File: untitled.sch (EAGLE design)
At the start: 22 parts, among them J3 CORTEX_DEBUG_PTH, J6 USB-MICROB, U1 ATSAMD21G-M, U2 MIC5501-3.0YM5-TR, U3 TPD2S017

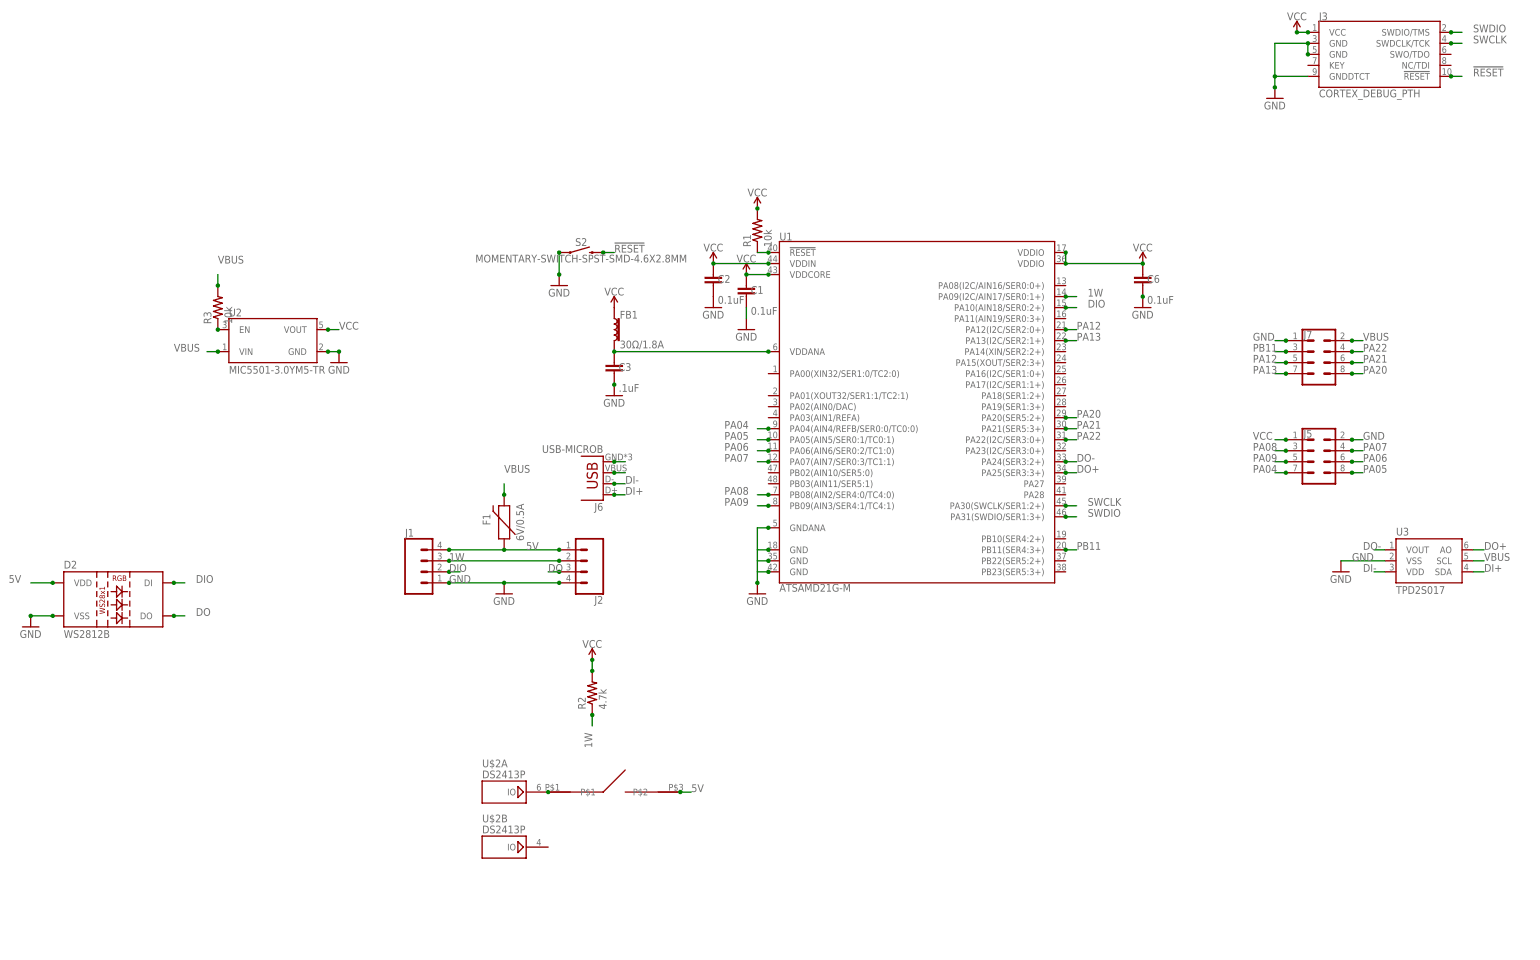
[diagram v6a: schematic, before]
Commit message: Updated Routing
Updated routing to remove vias. Changed switch wiring to reflect ds2413 example circuit.
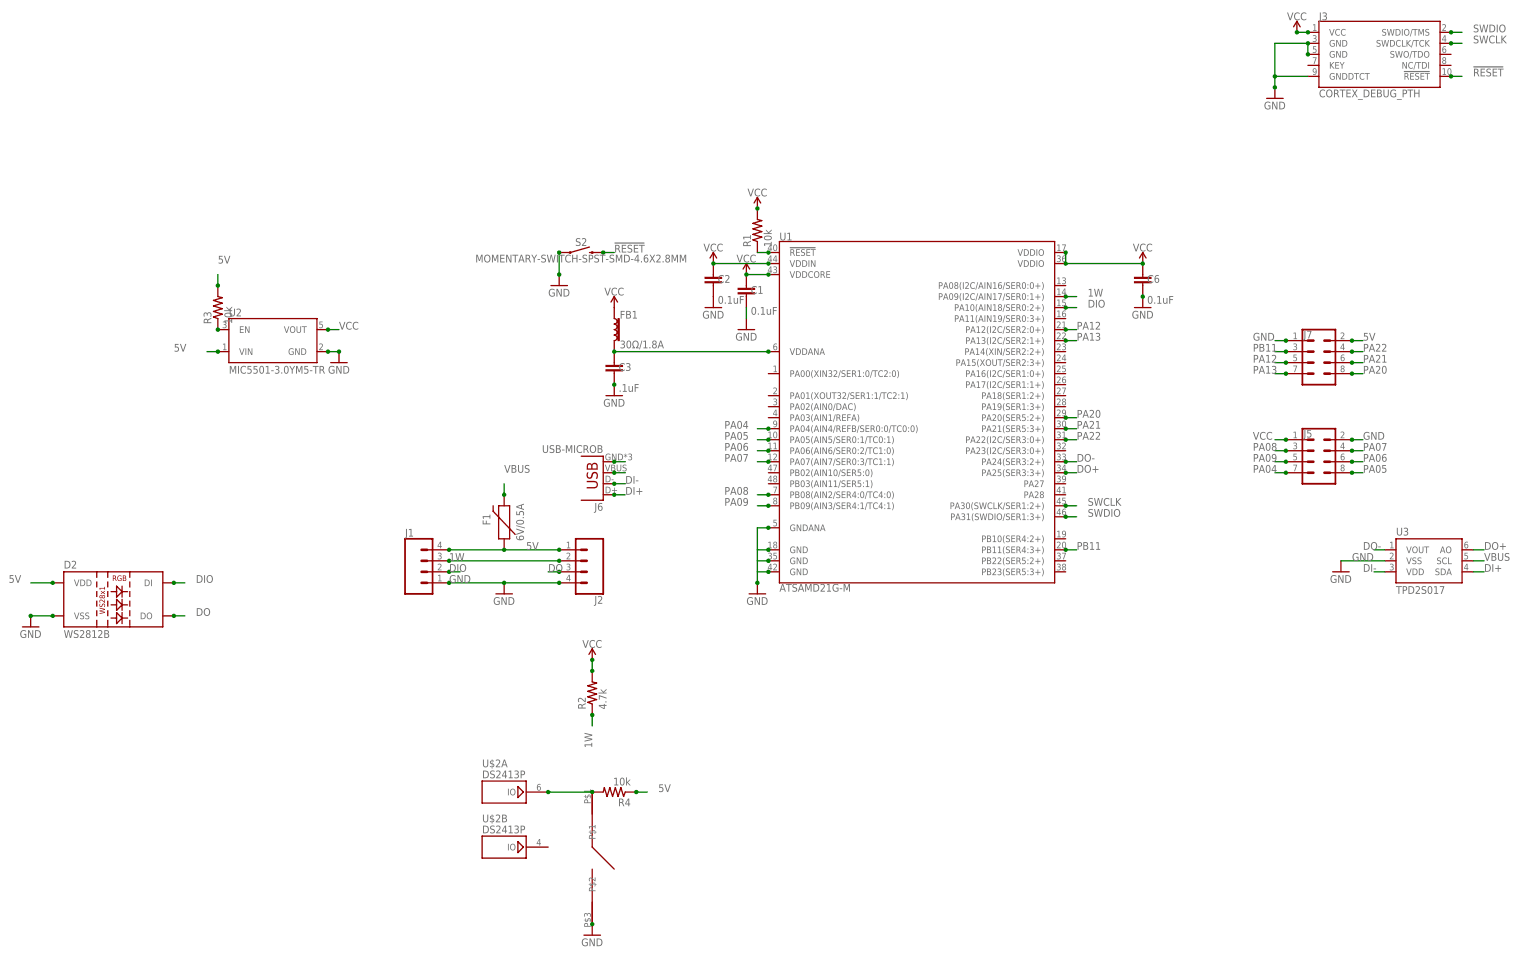
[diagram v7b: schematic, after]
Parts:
- added R4: 10k, rcl:R-US_R0402
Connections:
- net 5V: now also J7.2, R3.2, R4.1, U2.VIN; no longer U$1.P$2
- net GND: now also U$1.P$2
- net N$10: now also R4.2
- net VBUS: no longer J7.2, R3.2, U2.VIN
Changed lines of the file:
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@@
 <part name="GND3" library="supply1" library_urn="urn:adsk.eagle:library:371" deviceset="GND" device=""/>
 <part name="U3" library="SparkFun-IC-Conversion" library_urn="urn:adsk.eagle:library:522" deviceset="MCP4725" device="SOT-23" package3d_urn="urn:adsk.eagle:package:38775/1" value="TPD2S017"/>
+<part name="R4" library="rcl" library_urn="urn:adsk.eagle:library:334" deviceset="R-US_" device="R0402" package3d_urn="urn:adsk.eagle:package:23547/2" value="10k"/>
+<part name="GND10" library="supply1" library_urn="urn:adsk.eagle:library:371" deviceset="GND" device=""/>
 </parts>
 <sheets>
@@
 </plain>
 <instances>
-<instance part="U$1" gate="G$1" x="124.46" y="22.86" smashed="yes"/>
+<instance part="U$1" gate="G$1" x="119.38" y="7.62" smashed="yes" rot="R270"/>
 <instance part="J1" gate="G$1" x="81.28" y="73.66" smashed="yes">
 <attribute name="VALUE" x="76.2" y="66.294" size="1.778" layer="96" font="vector"/>
@@
 <attribute name="NAME" x="304.8" y="82.042" size="1.778" layer="95"/>
 <attribute name="VALUE" x="304.8" y="68.58" size="1.778" layer="96"/>
+</instance>
+<instance part="R4" gate="G$1" x="124.46" y="22.86" smashed="yes" rot="R180">
+<attribute name="NAME" x="128.27" y="21.3614" size="1.778" layer="95" rot="R180"/>
+<attribute name="VALUE" x="128.27" y="26.162" size="1.778" layer="96" rot="R180"/>
+</instance>
+<instance part="GND10" gate="1" x="119.38" y="-10.16" smashed="yes">
+<attribute name="VALUE" x="116.84" y="-12.7" size="1.778" layer="96"/>
 </instance>
 </instances>
@@
 <pinref part="GND11" gate="1" pin="GND"/>
 </segment>
+<segment>
+<pinref part="U$1" gate="G$1" pin="P$2"/>
+<pinref part="GND10" gate="1" pin="GND"/>
+<junction x="119.38" y="-7.62"/>
+</segment>
 </net>
 <net name="N$4" class="0">
@@
 </segment>
 </net>
-<net name="N$10" class="0">
-<segment>
-<pinref part="U$2" gate="A" pin="IO"/>
-<pinref part="U$1" gate="G$1" pin="P$1"/>
-<junction x="109.22" y="22.86"/>
-</segment>
-</net>
 <net name="DO" class="0">
 <segment>
@@
 </segment>
 <segment>
-<pinref part="U2" gate="G$1" pin="VIN"/>
-<wire x1="33.02" y1="124.46" x2="30.48" y2="124.46" width="0.1524" layer="91"/>
-<label x="22.86" y="124.46" size="1.778" layer="95"/>
-<junction x="33.02" y="124.46"/>
-</segment>
-<segment>
-<wire x1="294.64" y1="127" x2="297.18" y2="127" width="0.1524" layer="91"/>
-<label x="297.18" y="127" size="1.778" layer="95"/>
-<pinref part="J7" gate="G$1" pin="2"/>
-<junction x="294.64" y="127"/>
-</segment>
-<segment>
 <pinref part="U3" gate="U1" pin="SCL"/>
 <wire x1="322.58" y1="76.2" x2="325.12" y2="76.2" width="0.1524" layer="91"/>
 <label x="325.12" y="76.2" size="1.778" layer="95"/>
-</segment>
-<segment>
-<pinref part="R3" gate="G$1" pin="2"/>
-<wire x1="33.02" y1="139.7" x2="33.02" y2="142.24" width="0.1524" layer="91"/>
-<label x="33.02" y="144.78" size="1.778" layer="95"/>
-<junction x="33.02" y="139.7"/>
 </segment>
 </net>
@@
 </segment>
 <segment>
-<pinref part="U$1" gate="G$1" pin="P$2"/>
-<wire x1="139.7" y1="22.86" x2="142.24" y2="22.86" width="0.1524" layer="91"/>
-<label x="142.24" y="22.86" size="1.778" layer="95"/>
-<junction x="139.7" y="22.86"/>
+<pinref part="R4" gate="G$1" pin="1"/>
+<wire x1="129.54" y1="22.86" x2="132.08" y2="22.86" width="0.1524" layer="91"/>
+<label x="134.62" y="22.86" size="1.778" layer="95"/>
+<junction x="129.54" y="22.86"/>
+</segment>
+<segment>
+<pinref part="U2" gate="G$1" pin="VIN"/>
+<wire x1="33.02" y1="124.46" x2="30.48" y2="124.46" width="0.1524" layer="91"/>
+<label x="22.86" y="124.46" size="1.778" layer="95"/>
+<junction x="33.02" y="124.46"/>
+</segment>
+<segment>
+<pinref part="R3" gate="G$1" pin="2"/>
+<wire x1="33.02" y1="139.7" x2="33.02" y2="142.24" width="0.1524" layer="91"/>
+<label x="33.02" y="144.78" size="1.778" layer="95"/>
+<junction x="33.02" y="139.7"/>
+</segment>
+<segment>
+<wire x1="294.64" y1="127" x2="297.18" y2="127" width="0.1524" layer="91"/>
+<label x="297.18" y="127" size="1.778" layer="95"/>
+<pinref part="J7" gate="G$1" pin="2"/>
+<junction x="294.64" y="127"/>
 </segment>
 </net>
@@
 </segment>
 </net>
+<net name="N$10" class="0">
+<segment>
+<pinref part="U$2" gate="A" pin="IO"/>
+<pinref part="U$1" gate="G$1" pin="P$1"/>
+<wire x1="119.38" y1="22.86" x2="109.22" y2="22.86" width="0.1524" layer="91"/>
+<pinref part="R4" gate="G$1" pin="2"/>
+<junction x="119.38" y="22.86"/>
+<junction x="109.22" y="22.86"/>
+</segment>
+</net>

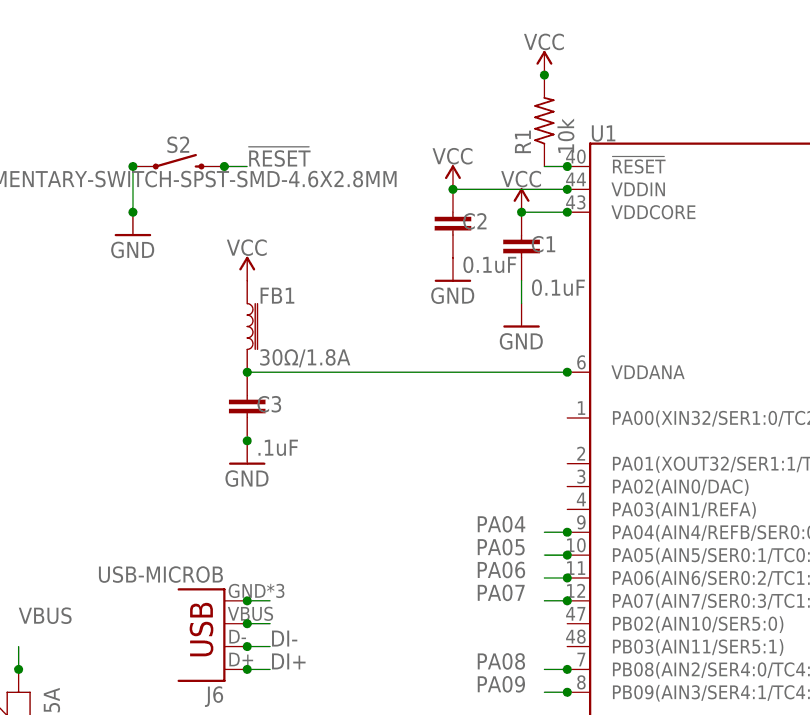
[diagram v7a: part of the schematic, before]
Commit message: added crystal
added a 32khz crystal per the arduino zero spec. updated routing to fit the crystal and caps.
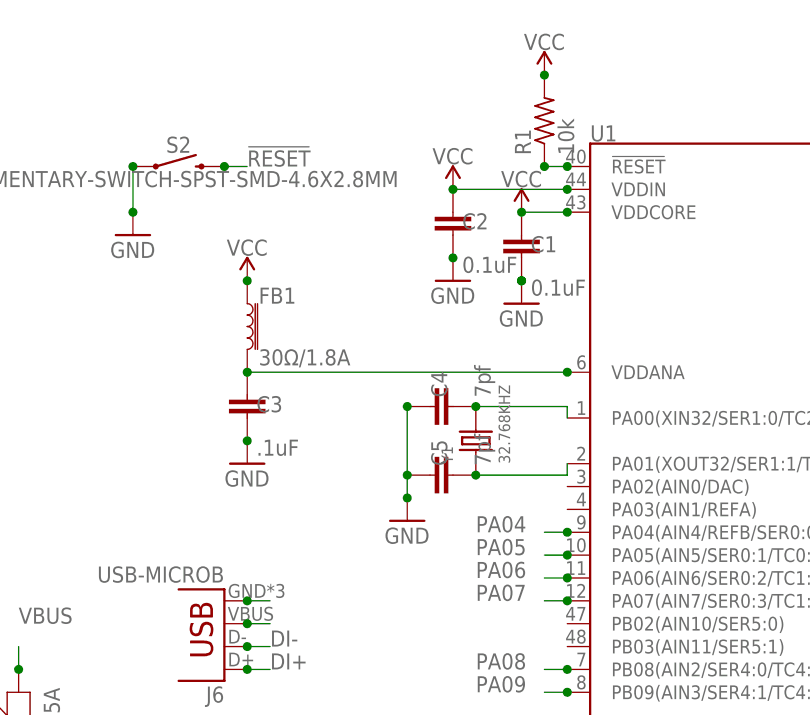
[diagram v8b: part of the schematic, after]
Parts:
- added C4, C5: 7pf, SparkFun-Capacitors:0.1UF-0402-16V-10%
- added Y1: 32.768KHZ, Seeed-Crystal Oscillator:SMD-CRYSTAL-ABS07-32.768KHZ-7PF-20PPM-70K(2P-3.2X1.5MM)
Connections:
- new net N$12: C5.2, U1.PA01(XOUT32/SER1:1/TC2:1), Y1.1
- new net N$13: C4.2, U1.PA00(XIN32/SER1:0/TC2:0), Y1.2
- net GND: now also C4.1, C5.1
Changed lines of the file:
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@@
 <layer number="115" name="ReferenceISLANDS" color="7" fill="1" visible="yes" active="yes"/>
 <layer number="116" name="Patch_BOT" color="9" fill="4" visible="no" active="yes"/>
+<layer number="117" name="BACKMAAT1" color="7" fill="1" visible="no" active="no"/>
 <layer number="118" name="Rect_Pads" color="7" fill="1" visible="no" active="yes"/>
+<layer number="119" name="KAP_TEKEN" color="7" fill="1" visible="no" active="no"/>
+<layer number="120" name="KAP_MAAT1" color="7" fill="1" visible="no" active="no"/>
 <layer number="121" name="_tsilk" color="7" fill="1" visible="no" active="yes"/>
 <layer number="122" name="_bsilk" color="7" fill="1" visible="no" active="yes"/>
@@
 <layer number="128" name="_bValues" color="7" fill="1" visible="no" active="yes"/>
 <layer number="129" name="Mask" color="7" fill="1" visible="no" active="yes"/>
+<layer number="130" name="SMDSTROOK" color="7" fill="1" visible="no" active="no"/>
 <layer number="131" name="tAdjust" color="7" fill="1" visible="no" active="yes"/>
 <layer number="132" name="bAdjust" color="7" fill="1" visible="no" active="yes"/>
+<layer number="133" name="bottom_silk" color="7" fill="1" visible="yes" active="yes"/>
+<layer number="134" name="silk_top" color="7" fill="1" visible="no" active="no"/>
+<layer number="135" name="silk_bottom" color="7" fill="1" visible="no" active="no"/>
+<layer number="136" name="silktop" color="7" fill="1" visible="no" active="yes"/>
+<layer number="137" name="silkbottom" color="7" fill="1" visible="no" active="yes"/>
 <layer number="144" name="Drill_legend" color="7" fill="1" visible="no" active="yes"/>
+<layer number="145" name="DrillLegend_01-16" color="7" fill="1" visible="no" active="yes"/>
+<layer number="146" name="DrillLegend_01-20" color="7" fill="1" visible="no" active="yes"/>
 <layer number="150" name="Notes" color="7" fill="1" visible="no" active="yes"/>
 <layer number="151" name="HeatSink" color="7" fill="1" visible="no" active="yes"/>
@@
 <part name="R4" library="rcl" library_urn="urn:adsk.eagle:library:334" deviceset="R-US_" device="R0402" package3d_urn="urn:adsk.eagle:package:23547/2" value="10k"/>
 <part name="GND10" library="supply1" library_urn="urn:adsk.eagle:library:371" deviceset="GND" device=""/>
+<part name="Y1" library="Seeed-Crystal Oscillator" library_urn="urn:adsk.eagle:library:466" deviceset="SMD-CRYSTAL-ABS07-32.768KHZ-7PF-20PPM-70K(2P-3.2X1.5MM)" device="" package3d_urn="urn:adsk.eagle:package:32493/1" value="32.768KHZ"/>
+<part name="C4" library="SparkFun-Capacitors" library_urn="urn:adsk.eagle:library:510" deviceset="0.1UF" device="-0402-16V-10%" package3d_urn="urn:adsk.eagle:package:37413/1" value="7pf"/>
+<part name="C5" library="SparkFun-Capacitors" library_urn="urn:adsk.eagle:library:510" deviceset="0.1UF" device="-0402-16V-10%" package3d_urn="urn:adsk.eagle:package:37413/1" value="7pf"/>
+<part name="GND13" library="supply1" library_urn="urn:adsk.eagle:library:371" deviceset="GND" device=""/>
 </parts>
 <sheets>
@@
 <attribute name="VALUE" x="144.78" y="132.08" size="1.778" layer="96"/>
 </instance>
-<instance part="GND2" gate="1" x="154.94" y="129.54" smashed="yes">
-<attribute name="VALUE" x="152.4" y="127" size="1.778" layer="96"/>
+<instance part="GND2" gate="1" x="154.94" y="132.08" smashed="yes">
+<attribute name="VALUE" x="152.4" y="129.54" size="1.778" layer="96"/>
 </instance>
 <instance part="GND4" gate="1" x="124.46" y="114.3" smashed="yes">
@@
 <instance part="GND10" gate="1" x="119.38" y="-10.16" smashed="yes">
 <attribute name="VALUE" x="116.84" y="-12.7" size="1.778" layer="96"/>
+</instance>
+<instance part="Y1" gate="G$1" x="149.86" y="116.84" smashed="yes" rot="R90">
+<attribute name="NAME" x="147.32" y="114.3" size="1.27" layer="95" ratio="10" rot="R90"/>
+<attribute name="VALUE" x="153.67" y="114.3" size="1.27" layer="96" ratio="10" rot="R90"/>
+</instance>
+<instance part="C4" gate="G$1" x="147.32" y="120.65" smashed="yes" rot="R90">
+<attribute name="NAME" x="146.685" y="121.666" size="1.778" layer="95" rot="R90"/>
+<attribute name="VALUE" x="151.511" y="121.666" size="1.778" layer="96" rot="R90"/>
+</instance>
+<instance part="C5" gate="G$1" x="147.32" y="113.03" smashed="yes" rot="R90">
+<attribute name="NAME" x="146.685" y="114.046" size="1.778" layer="95" rot="R90"/>
+<attribute name="VALUE" x="151.511" y="114.046" size="1.778" layer="96" rot="R90"/>
+</instance>
+<instance part="GND13" gate="1" x="142.24" y="107.95" smashed="yes">
+<attribute name="VALUE" x="139.7" y="105.41" size="1.778" layer="96"/>
 </instance>
 </instances>
@@
 <wire x1="160.02" y1="147.32" x2="157.48" y2="147.32" width="0.1524" layer="91"/>
 <junction x="160.02" y="147.32"/>
+<junction x="157.48" y="147.32"/>
 </segment>
 <segment>
@@
 <pinref part="FB1" gate="G$1" pin="1"/>
 <pinref part="SUPPLY2" gate="G$1" pin="VCC"/>
+<junction x="124.46" y="134.62"/>
 </segment>
 <segment>
@@
 <pinref part="C2" gate="G$1" pin="2"/>
 <pinref part="GND1" gate="1" pin="GND"/>
+<junction x="147.32" y="137.16"/>
 </segment>
 <segment>
 <pinref part="C1" gate="G$1" pin="2"/>
 <pinref part="GND2" gate="1" pin="GND"/>
-<wire x1="154.94" y1="132.08" x2="154.94" y2="134.62" width="0.1524" layer="91"/>
+<junction x="154.94" y="134.62"/>
+<junction x="154.94" y="134.62"/>
 </segment>
 <segment>
@@
 <junction x="119.38" y="-7.62"/>
 </segment>
+<segment>
+<pinref part="C5" gate="G$1" pin="1"/>
+<pinref part="GND13" gate="1" pin="GND"/>
+<wire x1="142.24" y1="110.49" x2="142.24" y2="113.03" width="0.1524" layer="91"/>
+<pinref part="C4" gate="G$1" pin="1"/>
+<wire x1="142.24" y1="120.65" x2="142.24" y2="113.03" width="0.1524" layer="91"/>
+<junction x="142.24" y="113.03"/>
+<junction x="142.24" y="120.65"/>
+<junction x="142.24" y="110.49"/>
+</segment>
 </net>
 <net name="N$4" class="0">
@@
 </segment>
 </net>
+<net name="N$12" class="0">
+<segment>
+<pinref part="U1" gate="G$1" pin="PA01(XOUT32/SER1:1/TC2:1)"/>
+<pinref part="Y1" gate="G$1" pin="1"/>
+<wire x1="160.02" y1="114.3" x2="160.02" y2="113.03" width="0.1524" layer="91"/>
+<wire x1="160.02" y1="113.03" x2="149.86" y2="113.03" width="0.1524" layer="91"/>
+<pinref part="C5" gate="G$1" pin="2"/>
+<junction x="149.86" y="113.03"/>
+</segment>
+</net>
+<net name="N$13" class="0">
+<segment>
+<pinref part="U1" gate="G$1" pin="PA00(XIN32/SER1:0/TC2:0)"/>
+<pinref part="Y1" gate="G$1" pin="2"/>
+<wire x1="160.02" y1="119.38" x2="160.02" y2="120.65" width="0.1524" layer="91"/>
+<wire x1="160.02" y1="120.65" x2="149.86" y2="120.65" width="0.1524" layer="91"/>
+<pinref part="C4" gate="G$1" pin="2"/>
+<junction x="149.86" y="120.65"/>
+</segment>
+</net>
